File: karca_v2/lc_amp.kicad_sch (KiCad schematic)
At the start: 16 parts, among them U10 TLV9301, U8 TS5A3159ADBVR, U9 AD8223

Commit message: modified sch
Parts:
- removed C18: 0.82u, Capacitor_SMD:C_1206_3216Metric, symbol Device:C
- removed L2: 4.7m, symbol Device:L
- removed TP19: TestPoint, symbol Connector:TestPoint
- added C20: 0.15u, Capacitor_SMD:C_1206_3216Metric, symbol Device:C
- added C3: 0.075u, Capacitor_SMD:C_1206_3216Metric, symbol Device:C
- added R108, R94: 860, symbol Device:R_US
- added R50: 1k, symbol Device:R_US
- added U30: TLV9301, Package_TO_SOT_SMD:SOT-23-5, symbol Amplifier_Operational:TLV9301xDBV
- added U34: TVS0701, symbol karca_lib:TVS0701
- R38: value 90 -> 1k
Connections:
- net GND: now also C3.1, U30.2 (V-)
- net IN1: now also R94.2, U34. (IN); no longer TP17.1, U9.2 (-IN)
- net IN2: now also R108.2, U34. (IN); no longer TP20.1, U9.3 (+IN)
- net OUT: now also C20.1, U30.1, U30.4 (-)
- net at TP18.1, U9.6 (OUT): now also R38.2; no longer R38.1
- new net: C3.2, R50.1, U30.3 (+)
- new net: R108.1, TP20.1, U9.3 (+IN)
- new net: R94.1, TP17.1, U9.2 (-IN)
- new net: C20.2, R38.1, R50.2
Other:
- note added: "12.9V maximum Clamping voltage"
- note added: "fc = 1.5kHz"
- note added: "limits inout current to 10mA"
- note removed: "20 ohm series resistance from inductor"
- note removed: "fc = 2.5kHz"
- moved on the sheet: D27, TP17, TP20

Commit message: updated
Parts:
- removed R108, R94: 860, symbol Device:R_US
- removed U34: TVS0701, symbol karca_lib:TVS0701
- added D1, D54: TVS0701, symbol Device:D_TVS
- added R107, R93: 1k, symbol Device:R_US
- added TP19: TestPoint, symbol Connector:TestPoint
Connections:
- net +5V: now also U30.5 (V+)
- net GND: now also D1.1 (A1), D54.1 (A1)
- net IN1: now also TP17.1, D1.2 (A2), R93.2
- net IN2: now also TP20.1, D54.2 (A2), R107.2
- net OUT: now also TP19.1
- net at U9.3 (+IN): now also R107.1; no longer TP20.1
- net at U9.2 (-IN): now also R93.1; no longer TP17.1
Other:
- note added: "20 ohm series resistance from inductor"
- note added: "TVS diodes clamp at 12.9V"
- note removed: "12.9V maximum Clamping voltage"
- note removed: "fc = 1.5kHz"
- note removed: "limits inout current to 10mA"
- moved on the sheet: D27, TP17, TP20

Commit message: Version alpha
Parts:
- removed D1, D54: TVS0701, symbol Device:D_TVS
- removed D27: D_Schottky, Diode_SMD:D_SMA, symbol Device:D_Schottky
- removed RV1: 30k, symbol Device:R_Potentiometer
- removed U10, U30: TLV9301, Package_TO_SOT_SMD:SOT-23-5, symbol Amplifier_Operational:TLV9301xDBV
- removed U9: AD8223, symbol karca_lib:AD8223
- added C74: 10u, Capacitor_Tantalum_SMD:CP_EIA-3216-18_Kemet-A, symbol Device:C
- added U16: ~, Package_SON:VSON-8-1EP_3x3mm_P0.65mm_EP1.65x2.4mm_ThermalVias, symbol karca_lib:TVS0701-7V
- added U33: AD8223, Package_SO:SOIC-8_3.9x4.9mm_P1.27mm, symbol karca_lib:AD8223
- added U4, U5: TLV9304xD, Package_SO:SO-14_3.9x8.65mm_P1.27mm, symbol Amplifier_Operational:TLV9304xD
- R18: renamed from R36; footprint (none) -> Resistor_SMD:R_1206_3216Metric
- R19: renamed from R37; footprint (none) -> Resistor_SMD:R_1206_3216Metric
- R20: renamed from R93; footprint (none) -> Resistor_SMD:R_1206_3216Metric
- R21: renamed from R38; footprint (none) -> Resistor_SMD:R_1206_3216Metric
- R22: renamed from R50; footprint (none) -> Resistor_SMD:R_1206_3216Metric
- R23: renamed from R107; footprint (none) -> Resistor_SMD:R_1206_3216Metric
- TP23: renamed from TP17; footprint (none) -> TestPoint:TestPoint_Pad_D2.0mm
- TP24: renamed from TP18; footprint (none) -> TestPoint:TestPoint_Pad_D2.0mm
- TP25: renamed from TP19; footprint (none) -> TestPoint:TestPoint_Pad_D2.0mm
- TP26: renamed from TP20; footprint (none) -> TestPoint:TestPoint_Pad_D2.0mm
- TP27: renamed from TP21; footprint (none) -> TestPoint:TestPoint_Pad_D2.0mm
- renumbered C20 to C7, C17 to C8, C3 to C9, U8 to U14
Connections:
- net +5V: now also C74.2, U33.7 (Vs+)
- net GND: now also C74.1, U16.7 (GND), U16.8 (GND), U33.4 (-Vs)
- net IN1: now also U16.3 (IN)
- net IN2: now also U16.4 (IN)
- net OUT: now also U4.6 (-), U4.7
- net at TP27.1: now also U33.5 (REF), U5.1, U5.3 (+)
- net at R18.1, R19.1: now also U33.1 (Rg)
- net at R21.2, TP24.1: now also U33.6 (OUT)
- net at U14.4: now also U33.8 (+RG)
- net at R20.1: now also U33.2 (-IN)
- net at R23.1: now also U33.3 (+IN)
- net at C9.2, R22.1: now also U4.5 (+)
- new net INAMP_VREF: U5.2 (-)
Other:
- note added: "fc = 1.5kHz"
- note removed: "20 ohm series resistance from inductor"
- moved on the sheet: C8

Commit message: discrete traces
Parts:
- removed U16: ~, Package_SON:VSON-8-1EP_3x3mm_P0.65mm_EP1.65x2.4mm_ThermalVias, symbol karca_lib:TVS0701-7V
- added U16, U17: TVS0701, Package_SON:VSON-8-1EP_3x3mm_P0.65mm_EP1.65x2.4mm, symbol karca_lib:TVS0701
- renumbered C7 to C18, C74 to C19, C8 to C20, C9 to C21, U33 to U15
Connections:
- net GND: now also U16. (GND), U17. (GND)
- net IN1: now also U16.1 (IN)
- net IN2: now also U17.1 (IN)

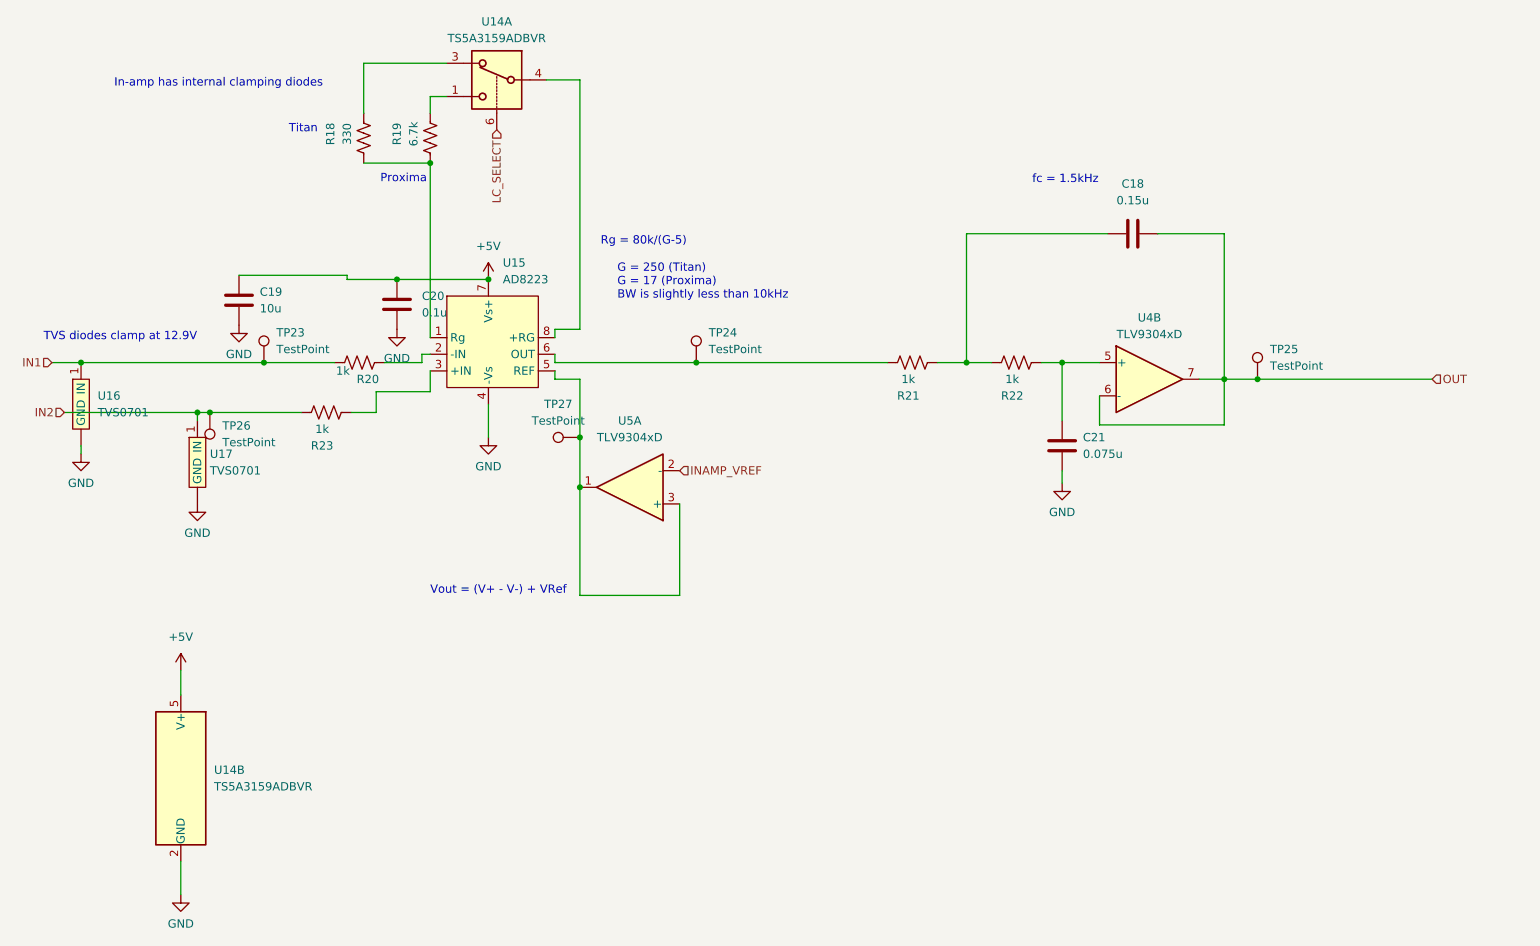
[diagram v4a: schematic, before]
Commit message: fixed TVS Diodes
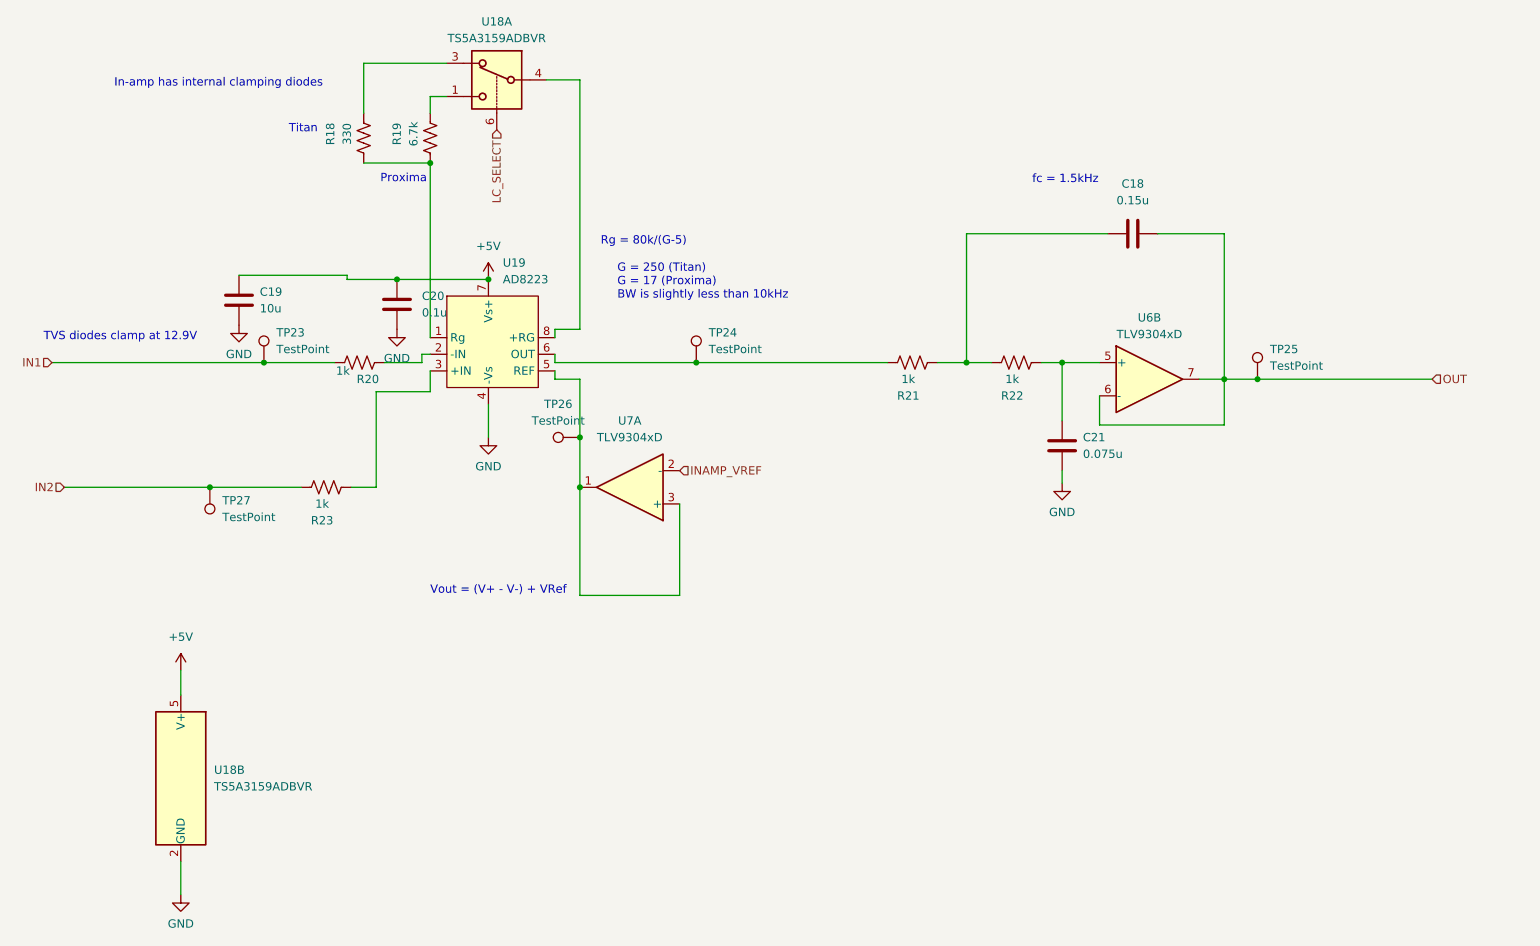
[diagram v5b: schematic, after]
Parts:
- removed U16, U17: TVS0701, Package_SON:VSON-8-1EP_3x3mm_P0.65mm_EP1.65x2.4mm, symbol karca_lib:TVS0701
- renumbered TP27 to TP26, TP26 to TP27, U14 to U18, U15 to U19, U4 to U6, U5 to U7
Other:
- moved on the sheet: R23, TP27

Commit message: Fixed ground capacitors
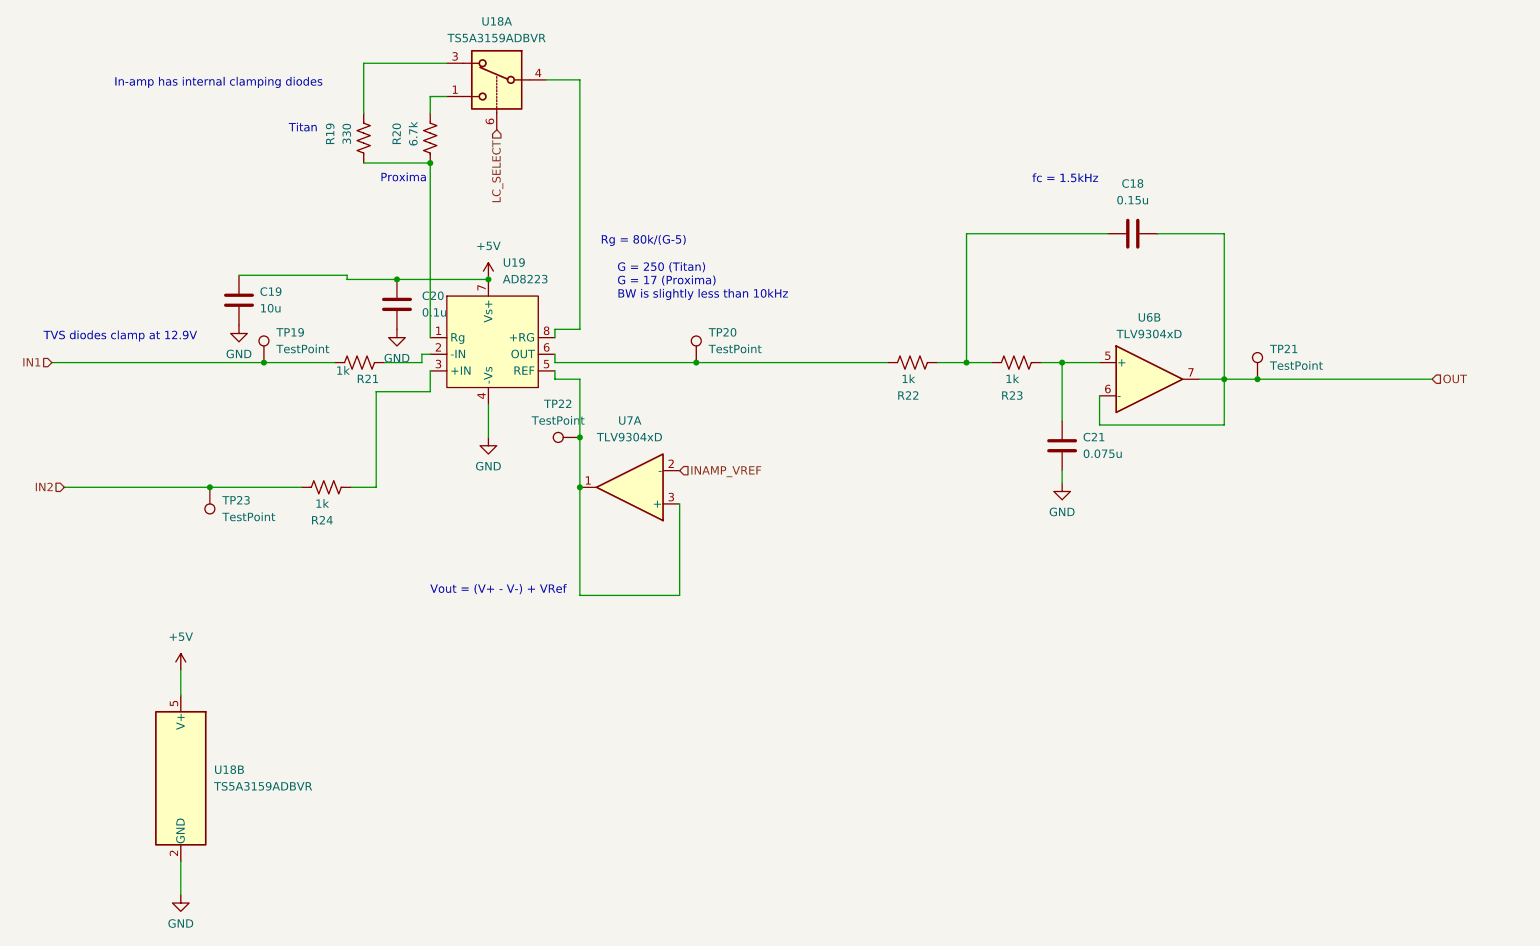
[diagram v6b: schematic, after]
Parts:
- renumbered R18 to R19, R19 to R20, R20 to R21, R21 to R22, R22 to R23, R23 to R24, TP23 to TP19, TP24 to TP20, TP25 to TP21, TP26 to TP22, TP27 to TP23
